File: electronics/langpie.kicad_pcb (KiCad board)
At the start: 2 copper layers, 100 x 100 mm, 62 parts, among them J1 USB_B_Micro, J2 Conn_01x04, J3 Conn_01x02, J4 Conn_01x02, J5 Conn_02x20_Odd_Even, J6 Conn_02x20_Odd_Even, Q1 2N7000, SW1 SW_SPDT, U1 DRV8833PWP, U2 MP1584, U3 CS5080E

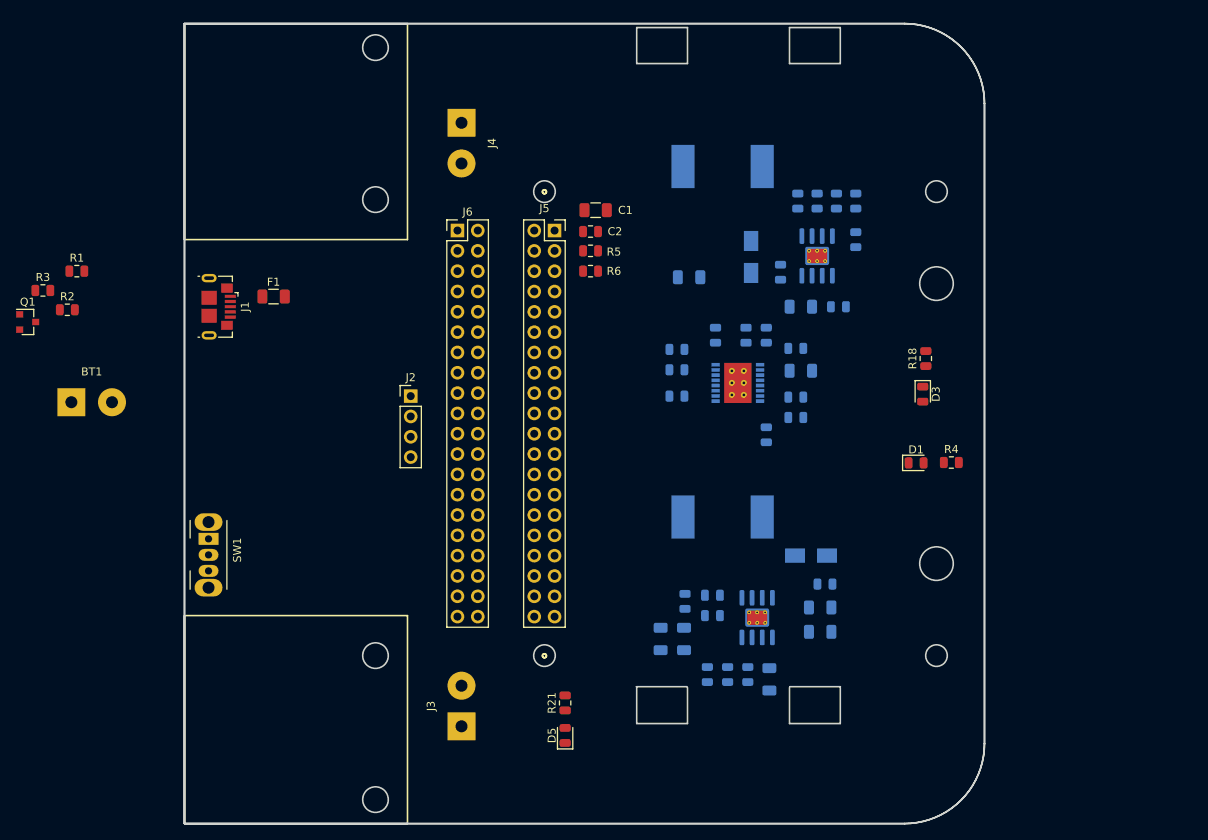
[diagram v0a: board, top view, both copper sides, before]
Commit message: Adding PCB and PCB library
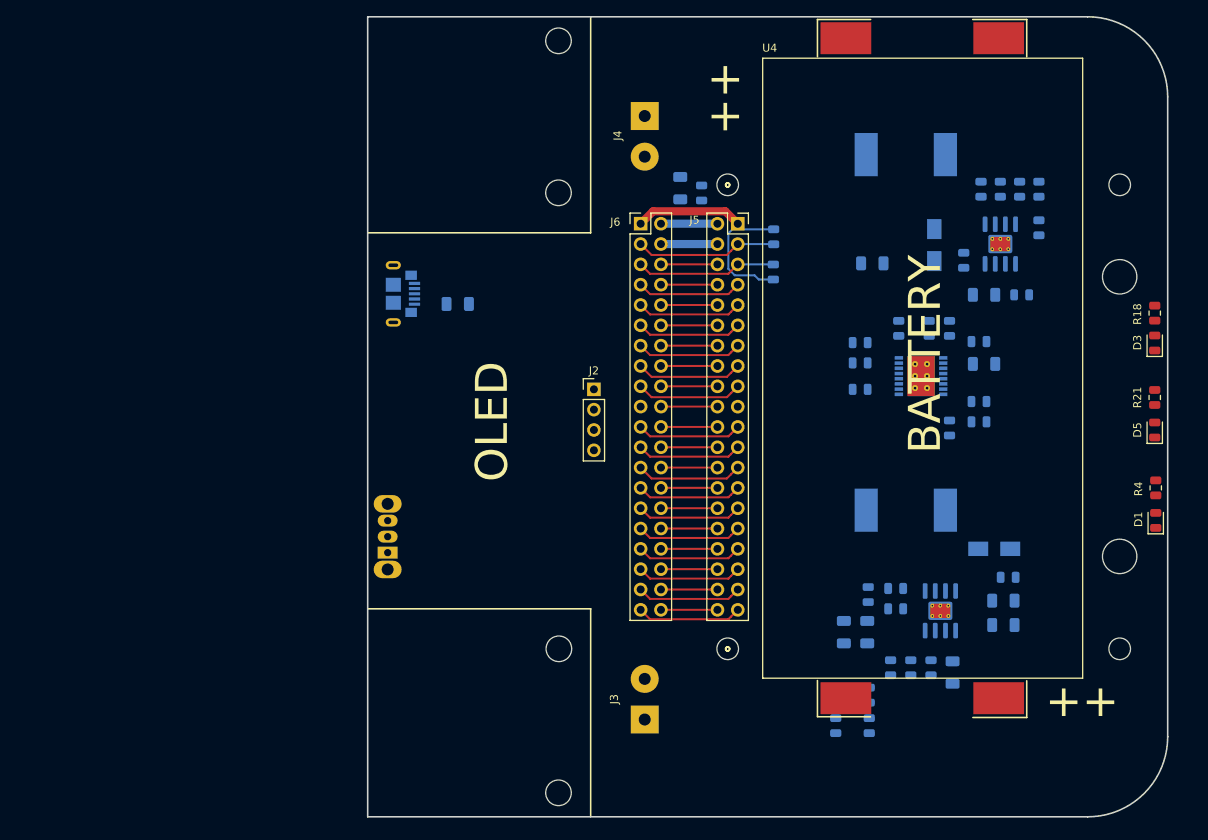
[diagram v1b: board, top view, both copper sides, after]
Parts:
- removed BT1: LiBattery, Connector_Wire:SolderWirePad_1x02_P5.08mm_Drill1.5mm
- added  : MountingHole_2.7mm_M2.5, MountingHole:MountingHole_2.7mm_M2.5, F.Cu at (142.4, 128.2)
- added  : MountingHole_3.2mm_M3, MountingHole:MountingHole_3.2mm_M3, F.Cu at (121.2, 146.2)
- added  : MountingHole_4.3mm_M4, MountingHole:MountingHole_4.3mm_M4, F.Cu at (191.4, 116.7)
- added  : MountingHole_4.3mm_M4, MountingHole:MountingHole_4.3mm_M4, F.Cu at (191.4, 81.7)
- added  : MountingHole_2.7mm_M2.5, MountingHole:MountingHole_2.7mm_M2.5, F.Cu at (191.4, 70.2)
- added  : MountingHole_2.7mm_M2.5, MountingHole:MountingHole_2.7mm_M2.5, F.Cu at (191.4, 128.2)
- added  : MountingHole_2.7mm_M2.5, MountingHole:MountingHole_2.7mm_M2.5, F.Cu at (142.4, 70.2)
- added  : MountingHole_3.2mm_M3, MountingHole:MountingHole_3.2mm_M3, F.Cu at (121.2, 52.2)
- added  : MountingHole_3.2mm_M3, MountingHole:MountingHole_3.2mm_M3, F.Cu at (121.2, 71.2)
- added  : MountingHole_3.2mm_M3, MountingHole:MountingHole_3.2mm_M3, F.Cu at (121.3, 128.2)
- added ?: , , F.Cu at (166.3, 82.9)
- added ?: , , F.Cu at (165.8, 83.4)
- added U4: 18650-Battery, langpie:li-battery-case, F.Cu at (146.7, 54.4)
- C1, C2, F1, J1, Q1, R1, R2, R3, R5, R6, SW1: moved to B.Cu
- moved R1 114.2 mm to (160.1, 137.8), turned to 90 degrees
- moved R3 113.0 mm to (155.9, 137.8), turned to 270 degrees
- moved Q1 111.9 mm to (156.6, 134.0), turned to 180 degrees
- moved R2 111.2 mm to (160.1, 134.0), turned to 90 degrees
- moved D5 83.0 mm to (195.7, 100.9)
- moved R21 83.0 mm to (195.7, 96.8)
- moved D1 30.8 mm to (195.9, 112.2), turned to 90 degrees
- moved D3 29.7 mm to (195.7, 90.0), turned to 90 degrees
- moved R18 29.2 mm to (195.7, 86.3), turned to 270 degrees
- moved R4 25.7 mm to (195.9, 108.1), turned to 270 degrees
- moved J1 23.1 mm to (101.8, 83.9), turned to 90 degrees
- moved F1 23.0 mm to (108.6, 85.1), turned to 180 degrees
- moved C11 23.0 mm to (160.4, 80.0)
- moved R5 23.0 mm to (148.1, 76.7), turned to 90 degrees
- moved C10 22.9 mm to (176.4, 70.8)
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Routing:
- net GND: track 0.00 -> 74.8 mm
- net /Motor Driver and RPi GPIO/3.3V: track 0.00 -> 43.8 mm
- net /Motor Driver and RPi GPIO/SDA.1: track 0.00 -> 17.8 mm
- net /Motor Driver and RPi GPIO/SCL.1: track 0.00 -> 17.6 mm
- net /DC DC Converter/5V: track 0.00 -> 14.1 mm
- net /Motor Driver and RPi GPIO/GPIO.3: track 0.00 -> 13.3 mm
- net /Motor Driver and RPi GPIO/SDA.0: track 0.00 -> 13.1 mm
- net /Motor Driver and RPi GPIO/SCLK: track 0.00 -> 13.1 mm
- net /Motor Driver and RPi GPIO/GPIO.25: track 0.00 -> 13.1 mm
- net /Motor Driver and RPi GPIO/GPIO.22: track 0.00 -> 13.1 mm
- net /Motor Driver and RPi GPIO/GPIO.2: track 0.00 -> 13.1 mm
- net /Motor Driver and RPi GPIO/MISO: track 0.00 -> 13.1 mm
- net /Motor Driver and RPi GPIO/GPIO.7: track 0.00 -> 13.1 mm
- net /Motor Driver and RPi GPIO/GPIO.24: track 0.00 -> 13.1 mm
- net /Motor Driver and RPi GPIO/GPIO.23: track 0.00 -> 13.1 mm
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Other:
- outline, holes or cut-outs redrawn

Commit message: Finish PCB, silightly change to SCH, Gerber generated, V1.0 HW almost done.
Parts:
- added ?: , , F.Cu at (228.9, 30.1)
- added ?: , , F.Cu at (239.8, 56.7)
- added ?: , , F.Cu at (155.1, -23.4)
- added ?: , , F.Cu at (-17.7, 90.1)
- moved C1 12.1 mm to (148.3, 68.1), turned to 90 degrees
- moved C2 10.0 mm to (148.9, 73.6), turned to 180 degrees
- moved R21 5.03 mm to (193.6, 101.3), turned to 270 degrees
- moved D5 4.19 mm to (193.6, 97.3), turned to 270 degrees
- moved D3 2.91 mm to (193.5, 91.9)
- moved R18 2.91 mm to (193.5, 88.2)
- moved D1 2.86 mm to (193.6, 110.5)
- moved R4 2.86 mm to (193.6, 106.4)
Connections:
- C13 pad 2: /Battery Charger/VBUS -> /USB_VBUS
- F1 pad 1: /Battery Charger/VBUS -> /USB_VBUS
- F1 pad 2: /USB_VBUS -> Net-(F1-Pad2)
- J1 pad 1: /USB_VBUS -> Net-(F1-Pad2)
- L2 pad 2: /Battery Charger/VBUS -> /USB_VBUS
- R19 pad 1: /Battery Charger/VBUS -> /USB_VBUS
- R20 pad 1: /Battery Charger/VBUS -> /USB_VBUS
- R21 pad 2: /Battery Charger/VBUS -> /USB_VBUS
- R23 pad 1: /Battery Charger/VBUS -> /USB_VBUS
- R4 pad 1: /Battery Charger/VBUS -> /USB_VBUS
- U2 pad 9: (no net) -> GND
- U3 pad 9: (no net) -> GND
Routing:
- net GND: track 74.8 -> 622.1 mm, vias 0 -> 21
- net /USB_VBUS: track 0.00 -> 274.7 mm, vias 0 -> 1
- net /DC DC Converter/EN: track 0.00 -> 236.6 mm, vias 0 -> 3
- net /Battery Charger/BATT: track 0.00 -> 162.1 mm, vias 0 -> 18
- net /DC DC Converter/5V: track 14.1 -> 168.7 mm, vias 0 -> 2
- net Net-(Q1-Pad3): track 0.00 -> 87.1 mm, vias 0 -> 2
- net /Motor Driver and RPi GPIO/Motor1_A: track 0.00 -> 63.5 mm, vias 0 -> 1
- net Net-(D5-Pad1): track 0.00 -> 63.4 mm, vias 0 -> 1
- net /Motor Driver and RPi GPIO/Motor1_B: track 0.00 -> 61.3 mm, vias 0 -> 1
- net /Motor Driver and RPi GPIO/Motor2_B: track 0.00 -> 58.2 mm, vias 0 -> 1
- net /Motor Driver and RPi GPIO/Motor2_A: track 0.00 -> 57.7 mm, vias 0 -> 1
- net /Motor Driver and RPi GPIO/GPIO.1: track 7.06 -> 55.7 mm, vias 0 -> 1
- net /Motor Driver and RPi GPIO/3.3V: track 43.8 -> 84.7 mm
- net /Motor Driver and RPi GPIO/GPIO.0: track 13.1 -> 50.7 mm, vias 0 -> 1
- net /Motor Driver and RPi GPIO/GPIO.3: track 13.3 -> 47.8 mm, vias 0 -> 1
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- added copper zone on B.Cu, net GND
- added copper zone on F.Cu, net GND
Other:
- board text added: "5V"
- board text added: "An Opensource Raspberray Pi Based Samart Car"
- board text added: "As RPi Pinout->"
- board text added: "Batteries has to match PCB +++ marks for polarities !!!"
- board text added: "CHG"
- board text added: "GITHUB https://github.com/langpie/langpie"
- board text added: "GND 5V SCL SCK"
- board text added: "Motor"
- board text added: "PWR SW"
- board text added: "USB CHG"
- board text added: "VUSB"

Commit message: Finalise the design and send to manufactory already for the V1
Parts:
- added G***: LOGO, langpie:logo, B.Cu at (113.4, 98.2)
- added REF**: OSHW-Logo2_14.6x12mm_SilkScreen, Symbol:OSHW-Logo2_14.6x12mm_SilkScreen, B.Cu at (190.4, 137.2)
- moved D1 4.40 mm to (193.6, 106.1), turned to 270 degrees
- moved R18 4.02 mm to (193.6, 92.2), turned to 90 degrees
- moved R4 3.73 mm to (193.6, 110.1), turned to 90 degrees
- moved D3 3.45 mm to (193.6, 88.5), turned to 270 degrees
- moved   1.00 mm to (121.2, 70.2)
- moved D5 0.11 mm to (193.6, 97.2)
- moved R21 0.10 mm to (193.6, 101.2)
- turned R11 to 270 degrees
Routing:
- net /DC DC Converter/EN: track 236.6 -> 229.1 mm
- net /DC DC Converter/5V: track 168.7 -> 172.1 mm
- net /Motor Driver and RPi GPIO/Motor1_B: track 61.3 -> 64.3 mm
- net (no net): track 2.80 -> 0.00 mm
- net GND: track 622.1 -> 619.7 mm, vias 21 -> 23
- net Net-(D5-Pad1): track 63.4 -> 61.2 mm
- net /Battery Charger/BATT: track 162.1 -> 160.1 mm
- net /Motor Driver and RPi GPIO/M2_in2: track 7.40 -> 5.37 mm
- net Net-(Q1-Pad3): track 87.1 -> 85.4 mm
- net /Motor Driver and RPi GPIO/GPIO.0: track 50.7 -> 51.9 mm
- net /Motor Driver and RPi GPIO/GPIO.3: track 47.8 -> 46.8 mm
- net /Motor Driver and RPi GPIO/GPIO.1: track 55.7 -> 56.6 mm
- net /Motor Driver and RPi GPIO/Motor1_A: track 63.5 -> 64.5 mm
- net Net-(R16-Pad2): track 10.3 -> 10.9 mm
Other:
- board text added: "+"
- board text added: "18650 Li-ion Battery * 2"
- board text added: "A"
- board text added: "An Opensource Raspberry Pi Based Smart Car Project."
- board text added: "Batteries have to match PCB ++ marks for polarities !!!"
- board text added: "Langpie V1.0 20-04-2020"
- board text added: "URL: langpie.github.io"
- board text removed: "An Opensource Raspberray Pi Based Samart Car"
- board text removed: "Batteries has to match PCB +++ marks for polarities !!!"
